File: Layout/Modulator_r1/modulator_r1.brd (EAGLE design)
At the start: 68.2 x 40.6 mm, 21 parts, among them IC1 FT232RL, U1 ATMEGA328P-AU, U2 TPS79933QDDCRQ1

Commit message: Layout progress.
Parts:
- added C10: 1n8, resistor:C0402
- added C11, C12: 12p, resistor:C0402
- added C13, C14, C18: 5p1, resistor:C0402
- added C15: 56p, resistor:C0402
- added C16: 39p, resistor:C0402
- added C17: 2p2, resistor:C0402
- added C19: 6p2, resistor:C0402
- added C20, C21, C22, C23, C24, C25, C26, C28, C29, C8, C9: 47n, resistor:C0402
- added C27: 100p, resistor:C0402
- added C4: 100nF, resistor:C0603
- added C5: 10nF, resistor:C0603
- added C6: 220n, resistor:C0402
- added C7: 10n, resistor:C0402
- added L2: FB, resistor:0207/10
- added L3, L6: 56n, resistor:R0402
- added L4, L5: 27n, resistor:R0402
- added L7: 15n, resistor:R0402
- added L8: 43n, resistor:R0402
- added L9: 22n, resistor:R0402
- added Q1: FA-20H, crystal:FA-20H
- added R1: 56K, resistor:R0402
- added R2: 18R, resistor:R0402
- L1: device resistor:0207/12 -> resistor:0207/10
- moved J$2 16.5 mm to (2.54, 27.9)
- moved J$1 12.7 mm to (2.54, 11.4)
- moved U2 10.5 mm to (27.9, 34.3)
- moved LED4 8.89 mm to (35.6, 7.62)
- moved JP1 7.73 mm to (39.4, 29.2)
- moved U$1 7.73 mm to (24.1, 20.3), turned to 180 degrees
- moved LED3 7.62 mm to (39.4, 7.62)
- moved C1 6.48 mm to (57.1, 39.4)
- moved U1 6.48 mm to (39.4, 20.3)
- moved LED2 6.35 mm to (43.2, 7.62)
- moved U$4 6.35 mm to (63.5, 41.9)
- moved U$5 6.35 mm to (5.08, 41.9)
- moved LED1 5.08 mm to (47.0, 7.62)
- moved C2 4.58 mm to (52.1, 35.6)
- moved L1 4.58 mm to (58.4, 33.0)
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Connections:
- new net CC_IO0: U$1.10
- new net CC_IO2: U$1.4
- new net CC_IO3: U$1.3
- new net CC_LNA_N: C13.2, L3.1, L4.1, U$1.20
- new net CC_LNA_P: C14.1, L3.2, L5.1, U$1.19
- new net CC_NRESET: U$1.2
- new net CC_RF_PA: C16.2, L6.2, U$1.17
- new net CC_VDD: C15.1, C20.1, C21.1, C22.1, C23.1, C24.1, C25.1, C26.1, C27.1, C28.1, C29.1, R2.2, U$1.1, U$1.12, U$1.13, U$1.15, U$1.22, U$1.25, U$1.27, U$1.28, U$1.5, U2.5
- new net N$10: C7.1, U$1.21
- new net N$11: C6.1, U$1.6
- new net N$12: C10.2, U$1.24
- new net N$13: C10.1, U$1.23
- new net N$14: C11.1, Q1.1, U$1.31
- new net N$15: C19.1, L8.1, L9.2
- new net N$16: C12.1, Q1.3, U$1.30
- new net N$17: C14.2, J$1.SIG, L4.2
- new net N$18: C17.1, C18.1, L7.1, L8.2
- new net N$19: C16.1, C17.2, L7.2
- new net N$21: C15.2, L6.1, R2.1
- new net N$4: C5.1, JP2.VBUS, L2.1
- new net N$5: C4.1, IC1.17
- new net N$6: J$2.SIG, L9.1
- new net N$7: R1.1, U$1.14
- new net N$8: C9.1, U$1.29
- new net N$9: C8.1, U$1.26
- net GND: now also C11.2, C12.2, C13.1, C18.2, C19.2, C20.2, C21.2, C22.2, C23.2, C24.2, C25.2, C26.2, C27.2, C28.2, C29.2, C4.2, C5.2, C6.2, C7.2, C8.2, C9.2, IC1.26, L5.2, Q1.2, Q1.4, R1.2
- net VCCIO: now also L2.2; no longer JP2.VBUS
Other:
- board size 68.2 x 40.6 mm -> 68.9 x 47 mm

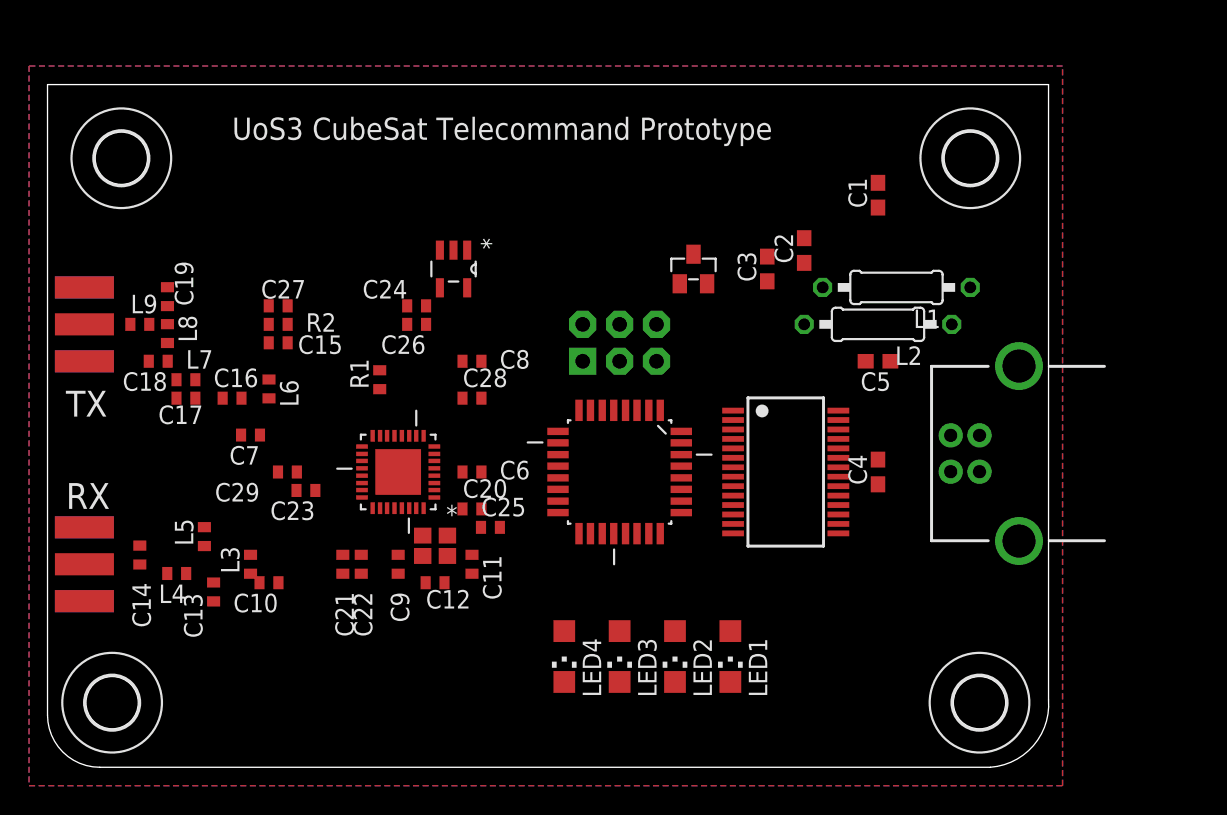
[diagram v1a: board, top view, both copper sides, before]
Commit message: Add USB power switch, start routing.
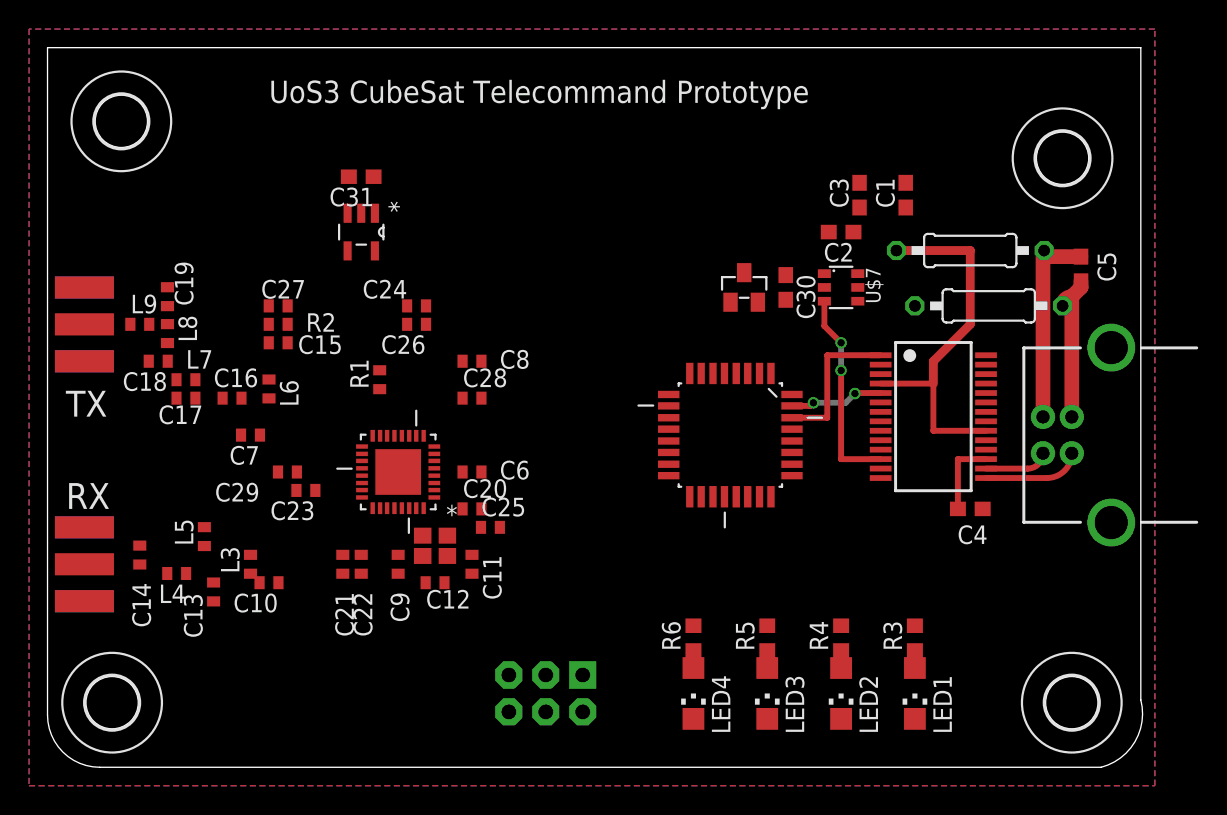
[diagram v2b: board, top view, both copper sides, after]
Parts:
- added C30, C31: 100nF, resistor:C0603
- added R3, R4, R5, R6: (no value), resistor:R0603
- added U$7: SIP32509DT-T1-GE3, phil-ic:SOT23-6
- moved JP1 24.7 mm to (34.3, 5.08), turned to 180 degrees
- moved C5 15.3 mm to (71.1, 34.3), turned to 90 degrees
- moved LED1 13.0 mm to (59.7, 5.08)
- moved LED2 11.7 mm to (54.6, 5.08)
- moved IC1 10.9 mm to (61.0, 24.1)
- moved LED3 10.5 mm to (49.5, 5.08)
- moved LED4 9.25 mm to (44.5, 5.08)
- moved L2 8.13 mm to (63.5, 35.6)
- moved C3 8.13 mm to (55.9, 39.4)
- moved U1 8.03 mm to (47.0, 22.9)
- moved C4 6.84 mm to (63.5, 17.8), turned to 0 degrees
- moved U2 6.84 mm to (21.6, 36.8)
- moved JP2 6.48 mm to (70.5, 22.9)
- moved L1 6.48 mm to (64.8, 31.8)
- moved U$3 6.35 mm to (70.5, 4.45)
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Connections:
- new net N$22: LED1.A, R3.1
- new net N$23: LED2.A, R4.1
- new net N$24: LED3.A, R5.1
- new net N$25: LED4.A, R6.1
- new net USB_NSLEEP: IC1.12, U$7.3
- new net VCC_LOGIC: C30.1, C31.1, U$6.3, U$7.1, U$7.2, U2.1
- net GND: now also C30.2, C31.2, U$7.4; no longer C5.2
- net N$3: now also C5.1
- net N$4: now also C5.2; no longer C5.1
- net VCCIO: now also U$7.5, U$7.6; no longer U$6.3, U2.1
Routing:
- net VCCIO: track 0.00 -> 25.8 mm
- net N$4: track 0.00 -> 14.5 mm
- net USB_NSLEEP: track 0.00 -> 14.1 mm, vias 0 -> 2
- net N$3: track 0.00 -> 11.4 mm
- net UART_TX: track 0.00 -> 10.4 mm
- net N$2: track 0.00 -> 6.61 mm
- net UART_RX: track 0.00 -> 6.47 mm, vias 0 -> 2
- net N$5: track 0.00 -> 5.36 mm
- net N$1: track 0.00 -> 4.36 mm
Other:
- board size 68.9 x 47 mm -> 75.4 x 49.5 mm

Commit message: Layout Modulator_r1
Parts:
- moved C8 15.3 mm to (22.9, 14.0), turned to 270 degrees
- moved L3 8.71 mm to (15.4, 22.6)
- moved C10 6.26 mm to (19.7, 17.1), turned to 0 degrees
- moved JP1 6.15 mm to (36.4, 10.8), turned to 270 degrees
- moved C28 5.68 mm to (28.8, 31.1), turned to 90 degrees
- moved C13 5.04 mm to (12.3, 17.0), turned to 0 degrees
- moved C7 3.71 mm to (16.4, 20.1)
- moved C23 2.35 mm to (16.4, 17.1)
- moved U1 2.18 mm to (48.5, 24.4)
- moved C29 1.94 mm to (16.4, 18.4)
- moved L5 1.90 mm to (8.98, 15.3), turned to 0 degrees
- moved C25 1.57 mm to (31.1, 18.0), turned to 90 degrees
- moved L4 0.55 mm to (9.00, 13.9)
- moved C20 0.30 mm to (29.4, 18.0), turned to 90 degrees
- moved C30 0.22 mm to (51.0, 32.9)
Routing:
- net CC_VDD: track 0.00 -> 63.3 mm
- net MOSI: track 0.00 -> 39.3 mm, vias 0 -> 4
- net VCC_LOGIC: track 0.00 -> 36.3 mm
- net AVR_NRESET: track 0.00 -> 34.3 mm
- net SCK: track 0.00 -> 34.3 mm, vias 0 -> 2
- net GND: track 0.00 -> 30.9 mm, vias 0 -> 2
- net MISO: track 0.00 -> 28.6 mm
- net +3V3: track 0.00 -> 28.5 mm
- net CC_LNA_P: track 0.00 -> 22.6 mm
- net NSS: track 0.00 -> 21.6 mm
- net CC_LNA_N: track 0.00 -> 20.3 mm
- net CC_RF_PA: track 0.00 -> 9.66 mm
- net N$16: track 0.00 -> 6.62 mm
- net VCCIO: track 25.8 -> 32.3 mm
- net N$14: track 0.00 -> 6.39 mm
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
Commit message: Add switches, general layout churn.
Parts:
- added C32, C33: 100nF, resistor:C0603
- added R10, R7, R8, R9: (no value), resistor:R0603
- added S1, S2, S3, S4, S5: SWITCH-MOMENTARY-2PTH, SparkFun-Electromechanical:TACTILE-PTH
- moved JP1 19.9 mm to (37.6, 30.7), turned to 180 degrees
- moved LED4 15.0 mm to (59.4, 3.95), turned to 270 degrees
- moved R6 11.7 mm to (55.1, 3.95), turned to 180 degrees
- moved LED1 10.5 mm to (59.4, 15.6), turned to 270 degrees
- moved LED3 10.4 mm to (59.5, 8.03), turned to 270 degrees
- moved LED2 8.19 mm to (59.4, 11.7), turned to 270 degrees
- moved R3 8.06 mm to (55.2, 15.6), turned to 180 degrees
- moved C25 7.92 mm to (25.0, 23.0), turned to 0 degrees
- moved C28 7.20 mm to (22.1, 28.5), turned to 0 degrees
- moved C2 6.69 mm to (56.6, 30.4)
- moved C20 5.93 mm to (25.0, 21.9), turned to 0 degrees
- moved C11 5.92 mm to (26.2, 19.1)
- moved C21 5.81 mm to (17.7, 19.2)
- moved C6 5.81 mm to (24.9, 24.2)
- moved C1 5.69 mm to (59.7, 33.7), turned to 0 degrees
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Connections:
- new net AVR_L1: R3.2, U1.23
- new net AVR_L2: R4.2, U1.24
- new net AVR_L3: R5.2, U1.25
- new net AVR_L4: R6.2, U1.26
- new net AVR_S1: R7.2, S1.1, U1.32
- new net AVR_S2: R8.2, S2.1, U1.1
- new net AVR_S3: R9.2, S3.1, U1.2
- new net AVR_S4: R10.2, S4.1, U1.9
- net +3V3: now also C32.1, C33.1, S1.3, S2.3, S3.3, S4.3
- net AVR_NRESET: now also S5.3
- net GND: now also C32.2, C33.2, R10.1, R7.1, R8.1, R9.1, S5.1
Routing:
- net +3V3: track 28.5 -> 75.8 mm
- net AVR_S1: track 0.00 -> 30.3 mm, vias 0 -> 1
- net AVR_L4: track 0.00 -> 22.1 mm, vias 0 -> 2
- net GND: track 30.9 -> 9.68 mm, vias 2 -> 10
- net AVR_S2: track 0.00 -> 19.8 mm, vias 0 -> 1
- net CC_VDD: track 63.3 -> 47.7 mm
- net AVR_L3: track 0.00 -> 14.9 mm, vias 0 -> 2
- net MOSI: track 39.3 -> 27.9 mm, vias 4 -> 2
- net AVR_L2: track 0.00 -> 11.3 mm, vias 0 -> 2
- net AVR_NRESET: track 34.3 -> 25.0 mm, vias 0 -> 2
- net AVR_S3: track 0.00 -> 9.10 mm, vias 0 -> 1
- net AVR_L1: track 0.00 -> 8.45 mm
- net VCCIO: track 32.3 -> 24.6 mm
- net UART_RX: track 11.5 -> 4.38 mm
- net CC_RF_PA: track 9.66 -> 3.29 mm
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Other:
- board text added: "L1"
- board text added: "L2"
- board text added: "L3"
- board text added: "L4"
- board text added: "RESET"

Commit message: Progress.
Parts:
- removed L1, L2: FB, resistor:0207/10
- added FB1, FB2: (no value), resistor:R0603
- moved U$4 2.84 mm to (70.3, 44.7)
- moved C5 2.77 mm to (68.2, 33.8), turned to 180 degrees
- moved C3 2.74 mm to (58.6, 34.9), turned to 90 degrees
- moved C32 2.61 mm to (47.7, 17.6), turned to 0 degrees
- moved C23 2.40 mm to (14.1, 19.9)
- moved C29 2.30 mm to (14.1, 21.0)
- moved C1 1.82 mm to (61.1, 34.9), turned to 90 degrees
- moved C7 1.44 mm to (14.1, 22.1)
- moved C22 0.50 mm to (18.9, 18.8)
- moved U$2 0.42 mm to (4.75, 4.75)
- moved C21 0.41 mm to (17.8, 18.8)
- moved C8 0.40 mm to (20.1, 18.8)
- moved C9 0.40 mm to (21.3, 18.8)
- moved U$5 0.36 mm to (4.88, 44.8)
- moved U$3 0.30 mm to (70.5, 4.75)
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- renumbered IC1 to U5, U$1 to U3, U$6 to U4, U$7 to U6
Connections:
- net GND: now also FB1.2; no longer L1.2
- net N$3: now also FB1.1; no longer L1.1
- net N$4: now also FB2.1; no longer L2.1
- net VCCIO: now also FB2.2; no longer L2.2
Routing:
- net AVR_S3: track 9.10 -> 35.2 mm, vias 1 -> 4
- net AVR_S4: track 2.14 -> 24.0 mm, vias 0 -> 2
- net AVR_S2: track 19.8 -> 38.1 mm, vias 1 -> 2
- net AVR_S1: track 30.3 -> 47.9 mm, vias 1 -> 2
- net GND: track 9.68 -> 5.47 mm, vias 10 -> 320
- net VCCIO: track 24.6 -> 28.3 mm
- net CC_VDD: track 47.7 -> 44.8 mm
- net CC_LNA_N: track 14.7 -> 16.6 mm
- net CC_LNA_P: track 16.6 -> 18.3 mm
- net N$17: track 3.90 -> 5.46 mm
- net N$10: track 4.61 -> 3.28 mm
- net USB_NSLEEP: track 14.7 -> 13.9 mm
- net +3V3: track 75.8 -> 76.6 mm
- net N$3: track 11.6 -> 12.1 mm
- net MISO: vias 2 -> 4
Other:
- board size 75.4 x 49.5 mm -> 75.2 x 49.5 mm
- board text added: "r1 - Sept 2015"
